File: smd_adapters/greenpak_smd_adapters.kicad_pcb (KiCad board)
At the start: 2 copper layers, 91.4 x 76.2 mm, 18 parts

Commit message: Fixed footprint library alias name.
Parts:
- REF** (x18): footprint smd_adapter:GREENPAK-SMD-ADAPTER-TSSOP-20 -> greenpack_smd_adapters:GREENPAK-SMD-ADAPTER-TSSOP-20

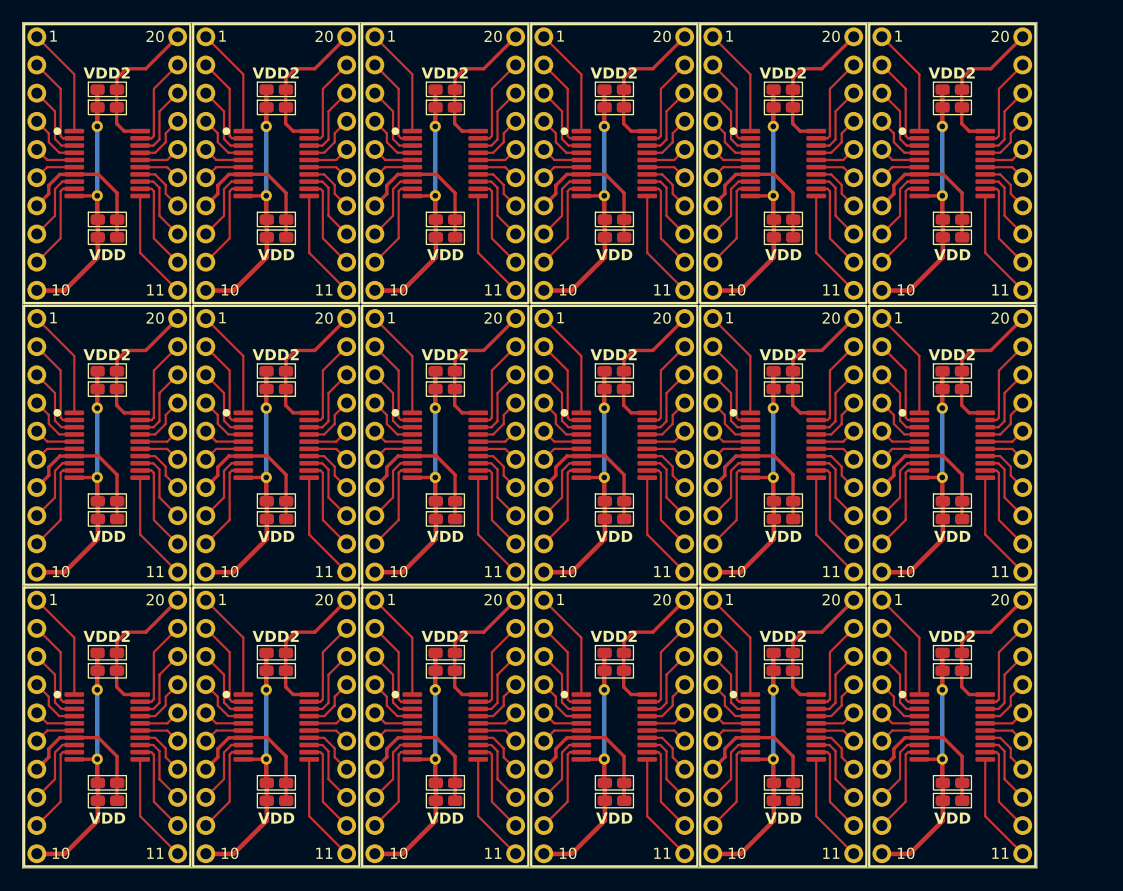
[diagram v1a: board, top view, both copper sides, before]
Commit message: Completed the STQFN-24 greenpak smd adapter.
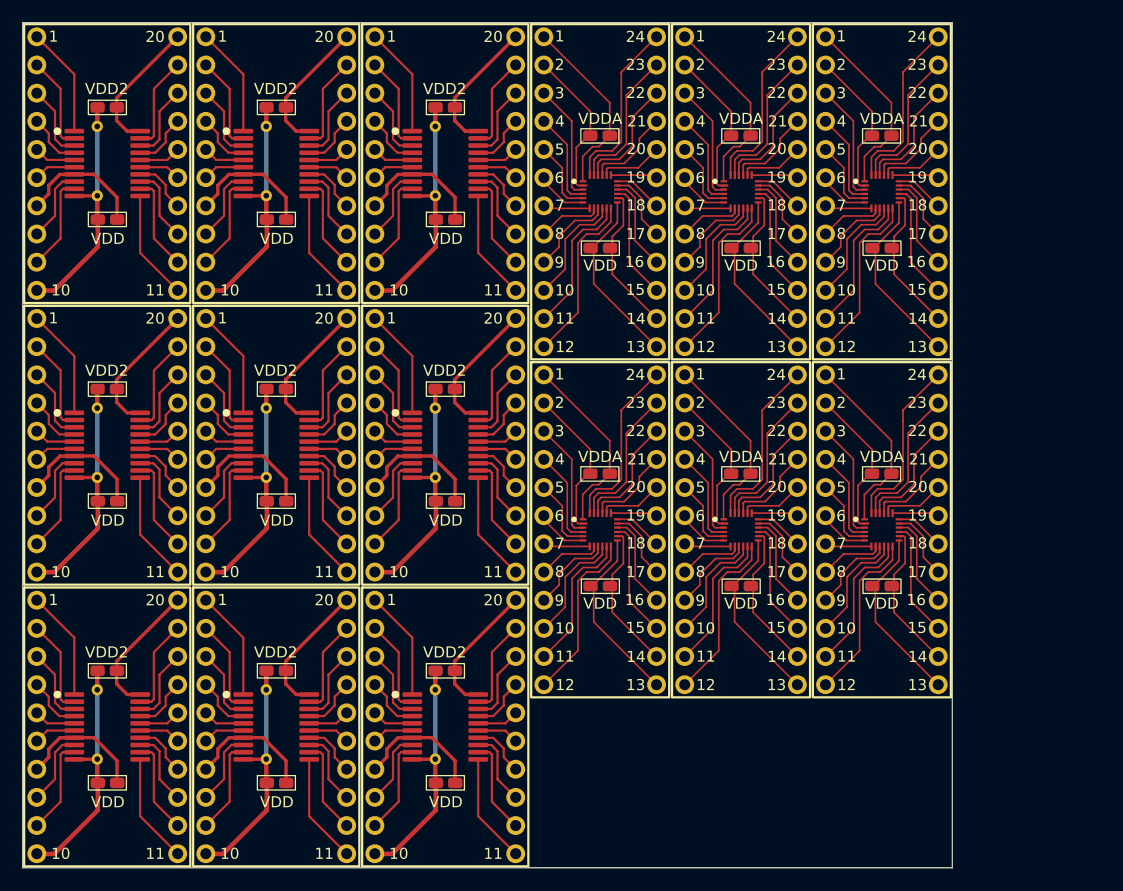
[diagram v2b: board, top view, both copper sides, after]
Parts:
- removed the REF** at (156.8, 62.9)
- removed the REF** at (156.8, 37.5)
- removed the REF** at (156.8, 88.3)
- removed the REF** at (141.6, 88.3)
- removed the REF** at (126.4, 62.9)
- removed the REF** at (141.6, 37.5)
- removed the REF** at (126.4, 88.3)
- removed the REF** at (141.6, 62.9)
- removed the REF** at (126.4, 37.5)
- added REF**: GREENPAK-SMD-ADAPTER-STQFN-24, greenpack_smd_adapters:GREENPAK-SMD-ADAPTER-STQFN-24, F.Cu at (125.1, 70.5)
- added REF**: GREENPAK-SMD-ADAPTER-STQFN-24, greenpack_smd_adapters:GREENPAK-SMD-ADAPTER-STQFN-24, F.Cu at (150.5, 40.0)
- added REF**: GREENPAK-SMD-ADAPTER-STQFN-24, greenpack_smd_adapters:GREENPAK-SMD-ADAPTER-STQFN-24, F.Cu at (150.5, 70.5)
- added REF**: GREENPAK-SMD-ADAPTER-STQFN-24, greenpack_smd_adapters:GREENPAK-SMD-ADAPTER-STQFN-24, F.Cu at (137.8, 70.5)
- added REF**: GREENPAK-SMD-ADAPTER-STQFN-24, greenpack_smd_adapters:GREENPAK-SMD-ADAPTER-STQFN-24, F.Cu at (125.1, 40.0)
- added REF**: GREENPAK-SMD-ADAPTER-STQFN-24, greenpack_smd_adapters:GREENPAK-SMD-ADAPTER-STQFN-24, F.Cu at (137.8, 40.0)
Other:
- board size 91.4 x 76.2 mm -> 83.8 x 76.2 mm

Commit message: More progress on the TSQFN-20 smd adapter.
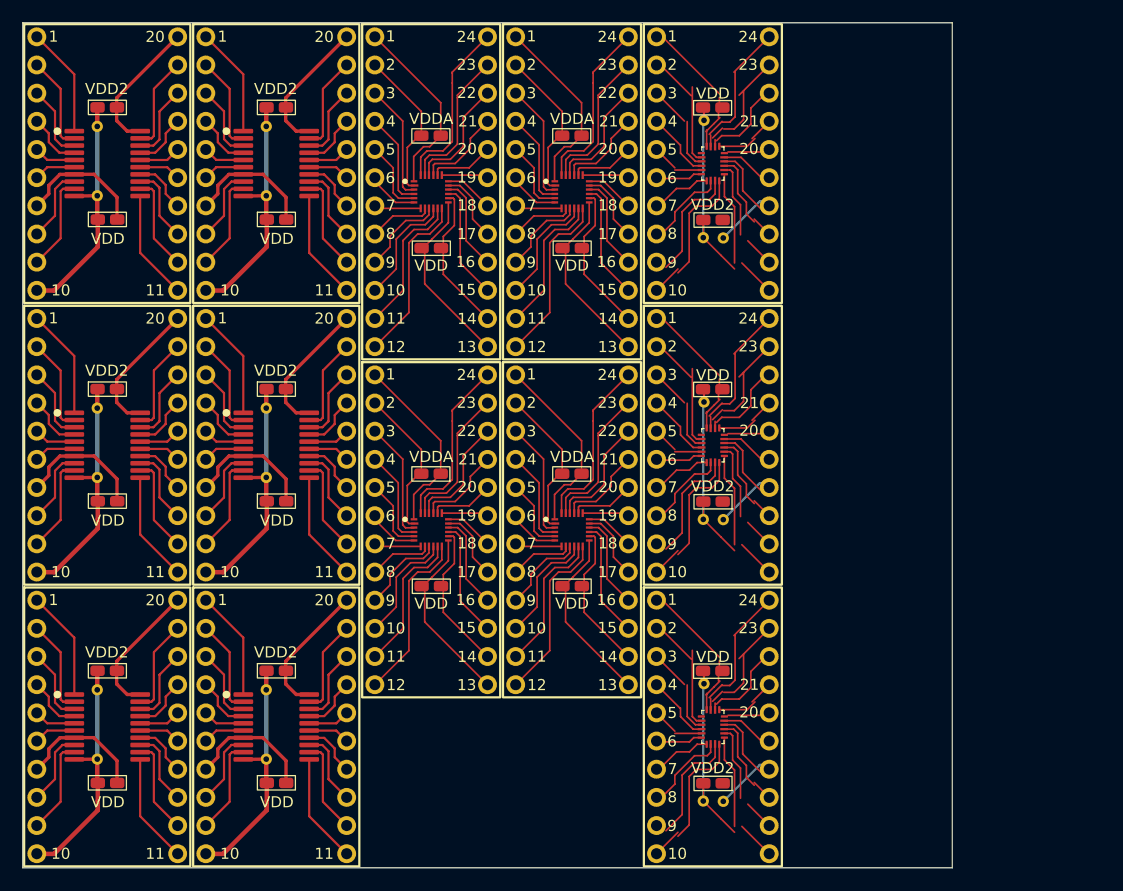
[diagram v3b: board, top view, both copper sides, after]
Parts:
- removed the REF** at (150.5, 40.0)
- removed the REF** at (150.5, 70.5)
- removed the REF** at (111.1, 88.3)
- removed the REF** at (111.1, 62.9)
- removed the REF** at (111.1, 37.5)
- added REF**: GREENPAK-SMD-ADAPTER-STQFN-20, greenpack_smd_adapters:GREENPAK-SMD-ADAPTER-STQFN-20, F.Cu at (135.3, 88.3)
- added REF**: GREENPAK-SMD-ADAPTER-STQFN-20, greenpack_smd_adapters:GREENPAK-SMD-ADAPTER-STQFN-20, F.Cu at (135.3, 62.9)
- added REF**: GREENPAK-SMD-ADAPTER-STQFN-20, greenpack_smd_adapters:GREENPAK-SMD-ADAPTER-STQFN-20, F.Cu at (135.3, 37.5)
- moved REF** 15.2 mm to (109.9, 70.5)
- moved REF** 15.2 mm to (109.9, 40.0)
- moved REF** 15.2 mm to (122.6, 70.5)
- moved REF** 15.2 mm to (122.6, 40.0)

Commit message: Completed the greenpak stqfn20 smd adapter.
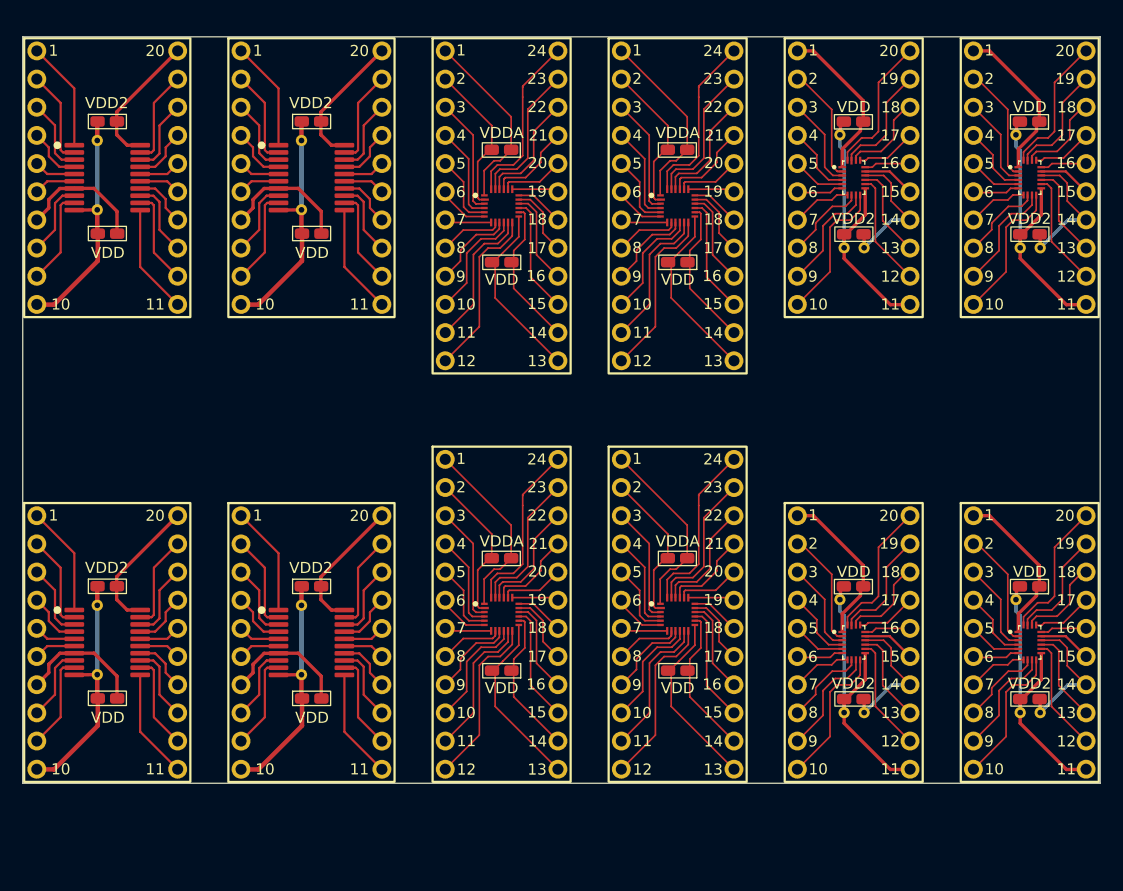
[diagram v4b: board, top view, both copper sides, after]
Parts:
- removed the REF** at (95.9, 62.9)
- removed the REF** at (80.6, 62.9)
- removed the REF** at (135.3, 62.9)
- added REF**: GREENPAK-SMD-ADAPTER-STQFN-20, greenpack_smd_adapters:GREENPAK-SMD-ADAPTER-STQFN-20, F.Cu at (163.8, 80.6)
- added REF**: GREENPAK-SMD-ADAPTER-STQFN-20, greenpack_smd_adapters:GREENPAK-SMD-ADAPTER-STQFN-20, F.Cu at (163.8, 38.7)
- moved REF** 14.8 mm to (148.0, 80.6)
- moved REF** 12.8 mm to (148.0, 38.7)
- moved REF** 12.2 mm to (132.1, 78.1)
- moved REF** 9.92 mm to (116.2, 78.1)
- moved REF** 9.61 mm to (132.1, 41.3)
- moved REF** 8.25 mm to (99.1, 80.7)
- moved REF** 7.62 mm to (80.6, 80.6)
- moved REF** 6.48 mm to (116.2, 41.3)
- moved REF** 3.42 mm to (99.1, 38.7)
- moved REF** 1.27 mm to (80.6, 38.7)
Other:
- board size 83.8 x 76.2 mm -> 97.2 x 67.3 mm

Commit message: Adjusted the greenpak smd adaptres. Generated gerbers.
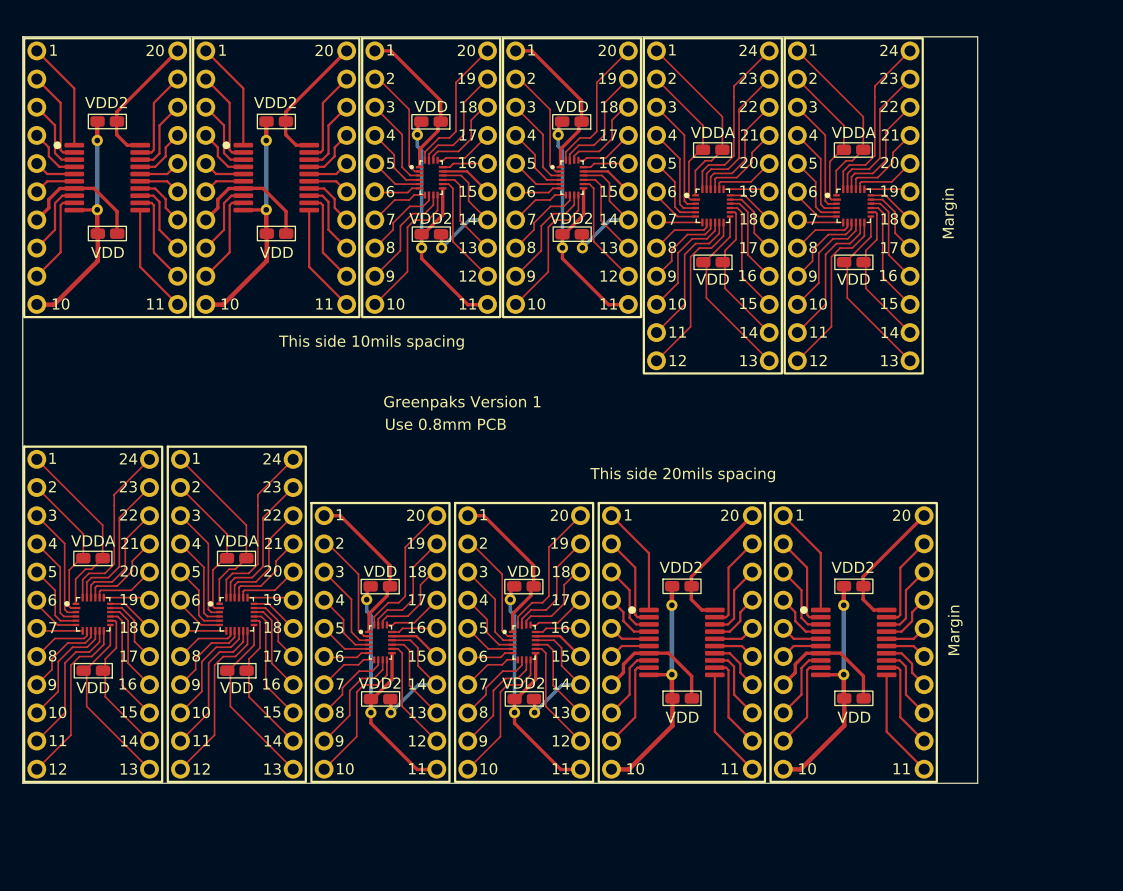
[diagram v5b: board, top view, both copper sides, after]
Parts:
- moved REF** 51.8 mm to (132.5, 80.6)
- moved REF** 48.9 mm to (148.0, 80.6)
- moved REF** 45.6 mm to (118.2, 80.6)
- moved REF** 42.7 mm to (105.3, 80.6)
- moved REF** 41.3 mm to (122.6, 38.7)
- moved REF** 39.8 mm to (92.3, 78.1)
- moved REF** 38.1 mm to (109.9, 38.7)
- moved REF** 36.8 mm to (79.4, 78.1)
- moved REF** 19.0 mm to (135.3, 41.3)
- moved REF** 15.9 mm to (148.0, 41.3)
- moved REF** 3.17 mm to (95.9, 38.7)
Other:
- board size 97.2 x 67.3 mm -> 86.1 x 67.3 mm
- board text added: "Greenpaks Version 1"
- board text added: "Margin"
- board text added: "This side 10mils spacing"
- board text added: "This side 20mils spacing"
- board text added: "Use 0.8mm PCB"
